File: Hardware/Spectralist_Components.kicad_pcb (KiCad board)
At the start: 4 copper layers, 70.8 x 100 mm, 98 parts, among them J1 Conn_01x12_Pin, J2 Conn_01x12_Pin, J3 Conn_01x10_Pin, J4 Conn_01x10_Pin, J5 Eurorack_10_pin_power, J6 SWD_Header, J7 Conn_01x02_Pin, U1 STM32H7B0VBTx, U2 PCM5100APW, U3 TPS561201, U4 LT1117-3.3, U5 MCP6002, U6 MX25LM51245G, U7 MCP6004, U8 TL072, Y1 8MHz 20pF

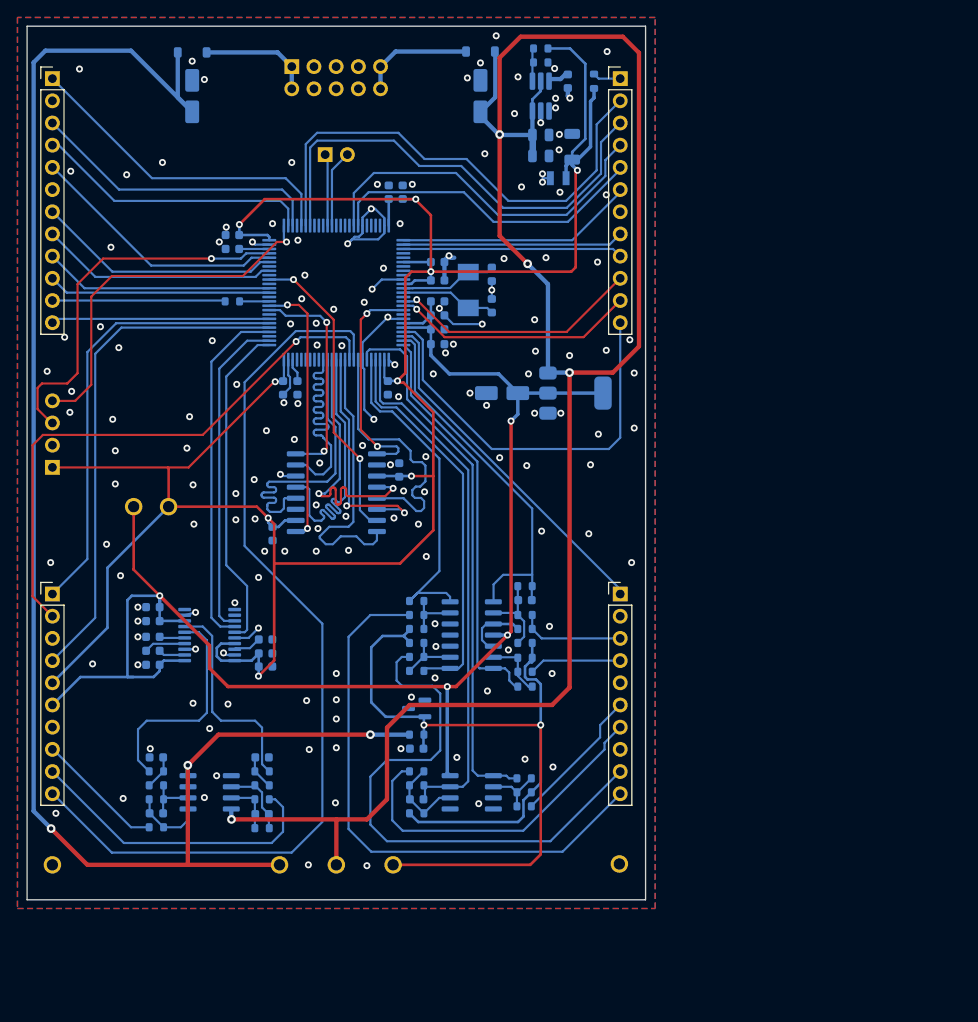
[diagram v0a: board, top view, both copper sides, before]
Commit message: Component PCB updates
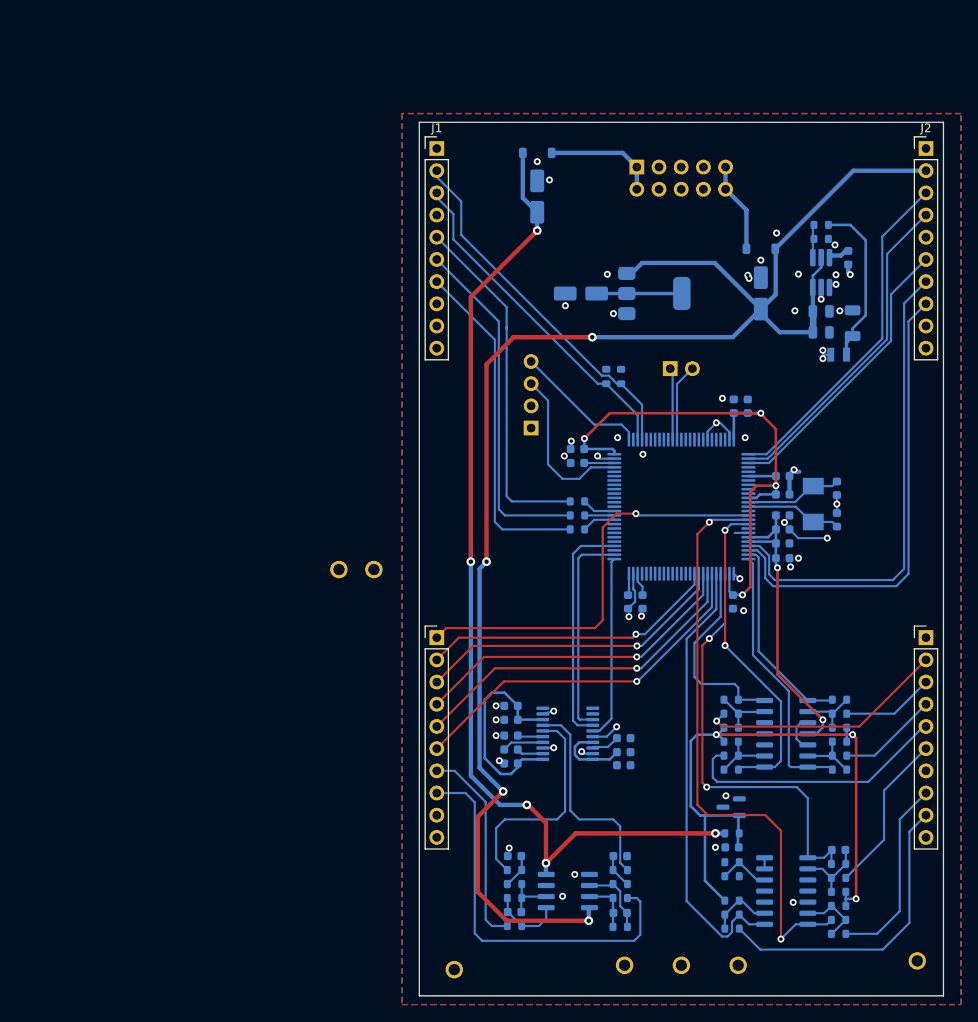
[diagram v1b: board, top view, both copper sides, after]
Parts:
- removed C33, C34: 100nF, Capacitor_SMD:C_0603_1608Metric
- removed C37: 2.2nF, Capacitor_SMD:C_0603_1608Metric
- removed U6: MX25LM51245G, Package_SO:SOIC-16W_7.5x10.3mm_P1.27mm
- added R28: 1k6, Resistor_SMD:R_0603_1608Metric, B.Cu at (123.1, 79.1)
- added R29: 75k, Resistor_SMD:R_0603_1608Metric, B.Cu at (148.1, 119.3)
- added R35: 82k, Resistor_SMD:R_0603_1608Metric, B.Cu at (148.1, 117.7)
- added R36: 47k, Resistor_SMD:R_0603_1608Metric, B.Cu at (148.1, 116.1)
- added R37: 10k, Resistor_SMD:R_0603_1608Metric, B.Cu at (135.8, 136.3)
- added R38: 1k, Resistor_SMD:R_0603_1608Metric, B.Cu at (118.1, 93.4)
- added R39: 1k, Resistor_SMD:R_0603_1608Metric, B.Cu at (118.1, 96.6)
- J1, J2: value Conn_01x12_Pin -> Conn_01x10_Pin; footprint Connector_PinHeader_2.54mm:PinHeader_1x12_P2.54mm_Vertical -> Connector_PinHeader_2.54mm:PinHeader_1x10_P2.54mm_Vertical
- R15: value 22 -> 1k6
- R31: value 100k -> 75k
- R32: value 20k -> 82k
- R33: value 33k -> 47k
- R34: value 6k8 -> 10k
- U1: value STM32H7B0VBTx -> STM32H723VGTx
- U5: value MCP6002 -> MCP6004; footprint Package_SO:SOIC-8_3.9x4.9mm_P1.27mm -> Package_SO:SO-14_3.9x8.65mm_P1.27mm
- moved J6 55.0 mm to (112.8, 85.0)
- moved R23 49.8 mm to (148.0, 136.5), turned to 0 degrees
- moved R22 49.1 mm to (148.0, 138.1), turned to 0 degrees
- moved R24 49.1 mm to (148.0, 134.9), turned to 0 degrees
- moved C35 48.6 mm to (148.0, 133.3), turned to 0 degrees
- moved TP4 47.5 mm to (104.0, 147.0)
- moved C14 46.5 mm to (147.8, 91.9)
- moved C15 46.5 mm to (147.8, 95.5)
- moved C21 46.5 mm to (118.1, 87.4)
- moved C16 46.5 mm to (137.6, 82.5)
- moved C17 46.5 mm to (141.6, 90.5)
- moved C18 46.5 mm to (141.6, 92.6)
- moved C19 46.5 mm to (135.9, 104.9)
- moved C20 46.5 mm to (123.9, 104.9)
- moved C22 46.5 mm to (136.0, 82.5)
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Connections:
- net /LED_Oct_B renamed /LED_Oct
- net /WarpCV renamed /Filter_B_CV
- net /Warp_CV_In renamed /Filter_B_CV_In
- net /Wavetable_Pos_A_Pot renamed /Harm_Stretch_Pot
- C35 pad 2: Net-(U5B--) -> Net-(U5A--)
- J1 pad 1: /LCD_SPI3_MOSI -> GND
- J1 pad 10: /Encoder_Up -> unconnected-(J1-Pin_10-Pad10)
- J1 pad 2: GND -> /I2C5_SCL
- J1 pad 3: /LCD_SPI3_SCK -> /I2C5_SDA
- J1 pad 4: /LCD_SPI3_SS -> GND
- J1 pad 5: /USB_DP -> /LED_Filter_A_Out
- J1 pad 6: GND -> /LED_Oct_Out
- J1 pad 7: /USB_DM -> /LED_Filter_B_Out
- J1 pad 8: /USB_VBUS -> unconnected-(J1-Pin_8-Pad8)
- J1 pad 9: /Encoder_Down -> unconnected-(J1-Pin_9-Pad9)
- J2 pad 1: /LCD_Backlight -> +3.3V
- J2 pad 10: /Warp_Amt_Trm -> unconnected-(J2-Pin_10-Pad10)
- J2 pad 2: /Octave_Up -> +12V
- J2 pad 3: /Octave_Down -> /Filter_Mode
- J2 pad 4: /LCD_DC -> /Warp_Mode
- J2 pad 5: /LCD_RESET -> GND
- J2 pad 6: /Mode -> /Octave_Btn
- J2 pad 7: GND -> /Filter_A_Trm
- J2 pad 8: /Warp_Polarity_Btn -> /Filter_A_Pot
- J2 pad 9: /Encoder_Btn -> unconnected-(J2-Pin_9-Pad9)
- J3 pad 1: /ChB_RM -> /Harm_Warp_Pot
- J3 pad 10: /Warp_Type_Pot -> unconnected-(J3-Pin_10-Pad10)
- J3 pad 3: GND -> /Harm_Stretch_Trm
- J3 pad 4: /ChB_Mix -> /Filter_Slope_Pot
- J3 pad 5: +3.3V -> /Filter_B_Trm
- J3 pad 6: +3.3VA -> /Filter_B_Pot
- J3 pad 7: GND -> /Audio_Out_L
- J3 pad 8: /Audio_Out_L -> /Audio_Out_R
- J3 pad 9: /Audio_Out_R -> unconnected-(J3-Pin_9-Pad9)
- J4 pad 1: /Wavetable_Pos_A_Trm -> unconnected-(J4-Pin_1-Pad1)
- J4 pad 10: /VCA_CV_In -> unconnected-(J4-Pin_10-Pad10)
- J4 pad 2: GND -> /Harm_Stretch_CV_In
- J4 pad 3: /Ext_Audio_In -> /Filter_A_CV_In
- J4 pad 5: GND -> /Filter_Slope_CV_In
- J4 pad 6: /Wavetable_Pos_A_CV_In -> /Pitch_CV_In
- J4 pad 7: /Pitch_CV_In -> unconnected-(J4-Pin_7-Pad7)
- J4 pad 8: GND -> /Harm_Warp_CV_In
- J4 pad 9: /Wavetable_Pos_B_CV_In -> /Pan_CV_In
- R12 pad 2: /Wavetable_Pos_B_CV_In -> /Filter_Slope_CV_In
- R15 pad 2: /LCD_Backlight -> /I2C5_SDA
- R16 pad 1: Net-(U5A--) -> Net-(U5B--)
- R17 pad 1: Net-(U5A--) -> Net-(U5B--)
- R17 pad 2: /Wavetable_Pos_A_CV_In -> /Harm_Warp_CV_In
- R19 pad 1: /WavetablePosA_CV -> /Harm_Warp_CV
- R19 pad 2: Net-(U5A--) -> Net-(U5B--)
- R21 pad 1: /WavetablePosB_CV -> /Filter_Slope_CV
- R22 pad 1: Net-(U5B--) -> Net-(U5A--)
- R23 pad 1: Net-(U5B--) -> Net-(U5A--)
- R24 pad 2: Net-(U5B--) -> Net-(U5A--)
- R26 pad 2: /VCA_CV_In -> /Harm_Stretch_CV_In
- R27 pad 1: /VcaCV -> /Harm_Stretch_CV
- R30 pad 2: /LED_Oct_B_Out -> /LED_Oct_Out
- R31 pad 1: /Ext_Audio_In -> Net-(U5C--)
- R31 pad 2: GND -> /-5V_REF
- R32 pad 1: Net-(U7A--) -> Net-(U5C--)
- R32 pad 2: /-5V_REF -> /Pan_CV_In
- R33 pad 1: Net-(U7A--) -> /Pan_CV
- R33 pad 2: /Ext_Audio_In -> Net-(U5C--)
- R34 pad 1: /AudioIn -> Net-(U5D-+)
- R34 pad 2: Net-(U7A--) -> +3.3V
- U1 pad 1: /Mode -> /Filter_Mode
- U1 pad 15: /Warp_Amt_Trm -> /Harm_Warp_Pot
- U1 pad 16: /Warp_Amt_Pot -> /Harm_Warp_CV
- U1 pad 17: /OCTOSPIM_P1_IO2 -> /Filter_Slope_CV
- U1 pad 2: /Warp_Polarity_Btn -> /Warp_Mode
- U1 pad 22: /Wavetable_Pos_B_Pot -> /Filter_A_Trm
- U1 pad 23: /Wavetable_Pos_A_Trm -> /Filter_A_Pot
- U1 pad 24: /AudioIn -> /Filter_A_CV
- U1 pad 29: /WavetablePosB_CV -> /Harm_Stretch_CV
- U1 pad 3: /Encoder_Btn -> /Octave_Btn
- U1 pad 30: /VcaCV -> /Pan_CV
- U1 pad 31: /WavetablePosA_CV -> /Filter_B_Pot
- U1 pad 32: GND -> /Filter_B_Trm
- U1 pad 33: /OCTOSPIM_P1_DQS -> /Filter_Slope_Pot
- U1 pad 34: /Warp_Type_Pot -> /Harm_Stretch_Trm
- U1 pad 36: /OCTOSPIM_P1_CLK -> unconnected-(U1-PB2-Pad36)
- U1 pad 37: /OCTOSPIM_P1_IO4 -> unconnected-(U1-PE7-Pad37)
- U1 pad 38: /OCTOSPIM_P1_IO5 -> unconnected-(U1-PE8-Pad38)
- U1 pad 39: /OCTOSPIM_P1_IO6 -> unconnected-(U1-PE9-Pad39)
- U1 pad 40: /OCTOSPIM_P1_IO7 -> unconnected-(U1-PE10-Pad40)
- U1 pad 41: /OCTOSPIM_P1_NCS -> unconnected-(U1-PE11-Pad41)
- U1 pad 55: /ChB_Mix -> unconnected-(U1-PD8-Pad55)
- U1 pad 56: /ChB_RM -> unconnected-(U1-PD9-Pad56)
- U1 pad 57: /B_Octave_Btn -> unconnected-(U1-PD10-Pad57)
- U1 pad 59: /OCTOSPIM_P1_IO1 -> unconnected-(U1-PD12-Pad59)
- U1 pad 60: /OCTOSPIM_P1_IO3 -> /LED_Filter_B
- U1 pad 62: unconnected-(U1-PD15-Pad62) -> /LED_Filter_A
- U1 pad 63: /Encoder_Up -> unconnected-(U1-PC6-Pad63)
- U1 pad 64: /Encoder_Down -> unconnected-(U1-PC7-Pad64)
- U1 pad 66: /OCTOSPIM_P1_IO0 -> unconnected-(U1-PC9-Pad66)
- U1 pad 77: /LCD_SPI3_SS -> unconnected-(U1-PA15(JTDI)-Pad77)
- U1 pad 78: /LCD_SPI3_SCK -> /I2C5_SDA
- U1 pad 79: unconnected-(U1-PC11-Pad79) -> /I2C5_SCL
- U1 pad 80: /LCD_SPI3_MOSI -> unconnected-(U1-PC12-Pad80)
- U1 pad 81: /Octave_Up -> unconnected-(U1-PD0-Pad81)
- U1 pad 82: /Octave_Down -> unconnected-(U1-PD1-Pad82)
- U1 pad 92: /LCD_DC -> unconnected-(U1-PB6-Pad92)
- U1 pad 93: /LCD_RESET -> unconnected-(U1-PB7-Pad93)
- U5 pad 1: /WavetablePosA_CV -> /Pitch_CV_Scaled
- U5 pad 4: GND -> +3.3VA
- U5 pad 7: /Pitch_CV_Scaled -> /Harm_Warp_CV
- U5 pad 8: +3.3VA -> /Pan_CV
- U7 pad 1: /AudioIn -> /Filter_A_CV
- U7 pad 14: /VcaCV -> /Harm_Stretch_CV
- U7 pad 8: /WavetablePosB_CV -> /Filter_Slope_CV
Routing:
- net +3.3V: track 282.4 -> 99.4 mm, vias 9 -> 4
- net /Warp_Type_Pot: track 107.1 -> 0.00 mm
- net +3.3VA: track 171.3 -> 69.6 mm, vias 4 -> 2
- net -12V: track 185.0 -> 113.8 mm, vias 3 -> 5
- net /Harm_Warp_CV: track 0.00 -> 67.4 mm, vias 0 -> 2
- net /VCA_CV_In: track 65.0 -> 0.00 mm
- net /Wavetable_Pos_B_CV_In: track 63.4 -> 0.00 mm
- net /WavetablePosA_CV: track 61.9 -> 0.00 mm
- net /ChB_Mix: track 58.3 -> 0.00 mm
- net /Octave_Up: track 56.9 -> 0.00 mm
- net /Filter_A_Trm: track 0.00 -> 55.1 mm
- net /Octave_Down: track 54.1 -> 0.00 mm
- net /Filter_A_Pot: track 0.00 -> 53.7 mm
- net /Pan_CV: track 0.00 -> 51.7 mm
- net /ChB_RM: track 51.5 -> 0.00 mm
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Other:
- board size 70.8 x 100 mm -> 60 x 100 mm
- board text added: "Spectralist v1.0 2025 Mountjoy Modular and Tal Shoshani"
- board text removed: "Kishoof v1.0 2024 Mountjoy Modular and Tal Shoshani"

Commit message: Started adding USB
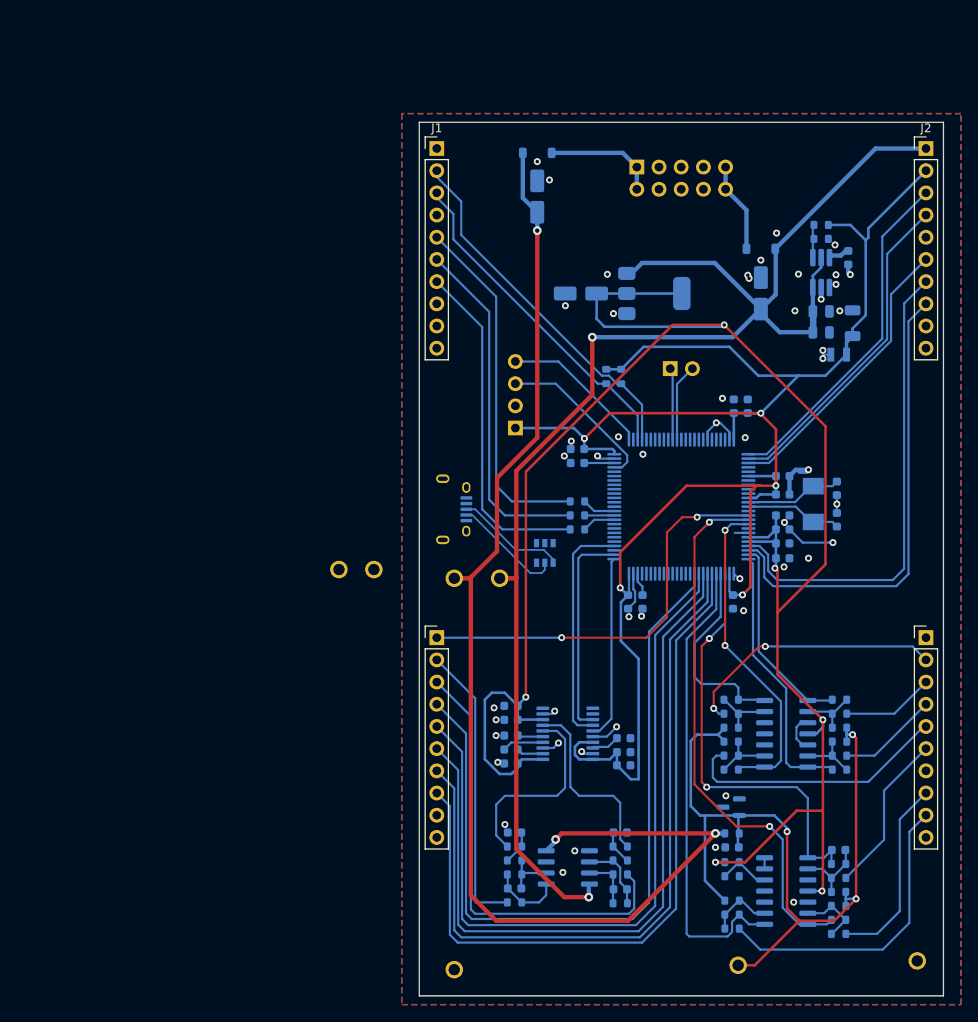
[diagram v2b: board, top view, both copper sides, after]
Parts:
- added J8: USB_B_Micro, Custom_Footprints:USB_Micro-B_Amphenol, B.Cu at (104.0, 94.3)
- added U6: STF202-22T1G, Custom_Footprints:STF202-22T1G, B.Cu at (114.4, 99.3)
- moved TP2 48.9 mm to (109.2, 102.2)
- moved TP3 48.4 mm to (104.0, 102.2)
- moved C31 2.70 mm to (110.9, 137.7)
- moved R10 2.70 mm to (123.0, 136.1)
- moved R7 2.70 mm to (110.9, 136.1)
- moved C29 2.70 mm to (110.9, 131.3)
- moved C30 2.70 mm to (123.0, 131.3)
- moved C32 2.70 mm to (123.0, 137.8)
- moved R3 2.70 mm to (110.9, 132.9)
- moved R4 2.70 mm to (123.0, 132.9)
- moved R5 2.70 mm to (110.9, 134.5)
- moved R6 2.70 mm to (123.0, 134.5)
- moved R8 2.70 mm to (123.0, 139.4)
- moved R9 2.70 mm to (110.9, 139.3)
- moved U8 2.70 mm to (117.0, 135.3)
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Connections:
- J2 pad 1: +3.3V -> +12V
- J2 pad 2: +12V -> +3.3V
- J3 pad 2: /Harm_Stretch_Pot -> /Audio_Out_L
- J3 pad 3: /Harm_Stretch_Trm -> /Audio_Out_R
- J3 pad 4: /Filter_Slope_Pot -> /Harm_Stretch_Pot
- J3 pad 5: /Filter_B_Trm -> /Harm_Stretch_Trm
- J3 pad 6: /Filter_B_Pot -> /Filter_Slope_Pot
- J3 pad 7: /Audio_Out_L -> /Filter_B_Trm
- J3 pad 8: /Audio_Out_R -> /Filter_B_Pot
- R34 pad 2: +3.3V -> +3.3VA
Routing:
- net +3.3VA: track 69.6 -> 221.6 mm, vias 2 -> 6
- net +3.3V: track 99.4 -> 207.1 mm, vias 4 -> 5
- net /Harm_Stretch_Pot: track 34.3 -> 87.1 mm, vias 1 -> 0
- net /Harm_Stretch_Trm: track 36.1 -> 86.6 mm, vias 1 -> 0
- net /Filter_Slope_Pot: track 38.1 -> 86.1 mm, vias 1 -> 0
- net /Filter_B_Trm: track 40.1 -> 85.5 mm, vias 1 -> 0
- net /Filter_B_Pot: track 42.0 -> 84.8 mm, vias 1 -> 0
- net -12V: track 113.8 -> 145.5 mm, vias 5 -> 3
- net /-5V_REF: track 73.1 -> 91.4 mm
- net +12V: track 174.7 -> 160.0 mm, vias 4 -> 2
- net /USB_D+: track 0.00 -> 12.7 mm
- net /USB_D-: track 0.00 -> 12.7 mm
- net /Audio_Out_L: track 23.3 -> 33.2 mm
- net /Audio_Out_R: track 44.8 -> 51.0 mm
- net /Harm_Warp_CV: track 67.4 -> 62.4 mm
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
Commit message: More layout on Component and Control boards
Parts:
- J1, J2: value Conn_01x10_Pin -> Conn_01x08_Pin; footprint Connector_PinHeader_2.54mm:PinHeader_1x10_P2.54mm_Vertical -> Connector_PinHeader_2.54mm:PinHeader_1x08_P2.54mm_Vertical
- moved TP5 73.1 mm to (153.0, 57.0)
- moved TP6 69.9 mm to (145.0, 57.0)
- moved TP2 60.2 mm to (149.0, 57.0)
- moved J8 57.6 mm to (130.0, 145.8), turned to 180 degrees
- moved TP3 56.9 mm to (139.0, 147.0)
- moved U6 11.9 mm to (107.9, 89.3)
- moved J3 10.0 mm to (102.0, 119.0)
- moved J4 10.0 mm to (158.0, 119.0)
- moved TP7 7.52 mm to (144.0, 147.0)
- moved J1 5.00 mm to (102.0, 58.0)
- moved J2 5.00 mm to (158.0, 58.0)
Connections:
- net /I2C5_SCL renamed /LED_SCL
- net /I2C5_SDA renamed /LED_SDA
- D3 pad 3: (no net) -> unconnected-(D3-NC-Pad3)
- J1 pad 7: /LED_Filter_B_Out -> GND
- J1 pad 8: unconnected-(J1-Pin_8-Pad8) -> /LED_Filter_B_Out
- J2 pad 1: +12V -> +3.3V
- J2 pad 2: +3.3V -> /Filter_Mode
- J2 pad 3: /Filter_Mode -> /Harmonic_Mode
- J2 pad 4: /Warp_Mode -> GND
- J2 pad 5: GND -> /Octave_Btn
- J2 pad 6: /Octave_Btn -> /Filter_A_Pot
- J2 pad 8: /Filter_A_Pot -> +12V
- J3 pad 1: /Harm_Warp_Pot -> /Filter_B_Trm
- J3 pad 10: unconnected-(J3-Pin_10-Pad10) -> /Harm_Warp_Pot
- J3 pad 3: /Audio_Out_R -> GND
- J3 pad 4: /Harm_Stretch_Pot -> /Audio_Out_R
- J3 pad 5: /Harm_Stretch_Trm -> /Filter_Slope_Pot
- J3 pad 6: /Filter_Slope_Pot -> /Filter_B_Pot
- J3 pad 7: /Filter_B_Trm -> GND
- J3 pad 8: /Filter_B_Pot -> /Harm_Stretch_Trm
- J3 pad 9: unconnected-(J3-Pin_9-Pad9) -> /Harm_Stretch_Pot
- J4 pad 1: unconnected-(J4-Pin_1-Pad1) -> GND
- J4 pad 10: unconnected-(J4-Pin_10-Pad10) -> /Filter_A_CV_In
- J4 pad 2: /Harm_Stretch_CV_In -> /Harm_Warp_CV_In
- J4 pad 3: /Filter_A_CV_In -> /Filter_B_CV_In
- J4 pad 4: /Filter_B_CV_In -> GND
- J4 pad 6: /Pitch_CV_In -> /Pan_CV_In
- J4 pad 7: unconnected-(J4-Pin_7-Pad7) -> GND
- J4 pad 8: /Harm_Warp_CV_In -> /Pitch_CV_In
- J4 pad 9: /Pan_CV_In -> /Harm_Stretch_CV_In
- J8 pad 1: unconnected-(J8-VBUS-Pad1) -> /USB_VBUS
- R12 pad 2: /Filter_Slope_CV_In -> /Pan_CV_In
- R13 pad 1: /Filter_B_CV -> /Filter_Slope_CV
- R17 pad 2: /Harm_Warp_CV_In -> /Harm_Stretch_CV_In
- R19 pad 1: /Harm_Warp_CV -> /Harm_Stretch_CV
- R20 pad 2: /Filter_B_CV_In -> /Filter_Slope_CV_In
- R21 pad 1: /Filter_Slope_CV -> /Pan_CV
- R26 pad 2: /Harm_Stretch_CV_In -> /Harm_Warp_CV_In
- R27 pad 1: /Harm_Stretch_CV -> /Harm_Warp_CV
- R32 pad 2: /Pan_CV_In -> /Filter_A_CV_In
- R33 pad 1: /Pan_CV -> /Filter_A_CV
- R35 pad 2: /Filter_A_CV_In -> /Filter_B_CV_In
- R36 pad 1: /Filter_A_CV -> /Filter_B_CV
- U1 pad 15: /Harm_Warp_Pot -> /Filter_B_Trm
- U1 pad 16: /Harm_Warp_CV -> /Harm_Stretch_CV
- U1 pad 17: /Filter_Slope_CV -> /Pan_CV
- U1 pad 2: /Warp_Mode -> /Harmonic_Mode
- U1 pad 22: /Filter_A_Trm -> /Filter_A_Pot
- U1 pad 23: /Filter_A_Pot -> /Filter_A_Trm
- U1 pad 24: /Filter_A_CV -> /Filter_B_CV
- U1 pad 25: /Filter_B_CV -> /Filter_Slope_CV
- U1 pad 29: /Harm_Stretch_CV -> /Harm_Warp_CV
- U1 pad 30: /Pan_CV -> /Filter_A_CV
- U1 pad 31: /Filter_B_Pot -> /Harm_Warp_Pot
- U1 pad 32: /Filter_B_Trm -> /Harm_Stretch_Pot
- U1 pad 33: /Filter_Slope_Pot -> /Harm_Stretch_Trm
- U1 pad 34: /Harm_Stretch_Trm -> /Filter_B_Pot
- U1 pad 35: /Harm_Stretch_Pot -> /Filter_Slope_Pot
- U5 pad 7: /Harm_Warp_CV -> /Harm_Stretch_CV
- U5 pad 8: /Pan_CV -> /Filter_A_CV
- U7 pad 1: /Filter_A_CV -> /Filter_B_CV
- U7 pad 14: /Harm_Stretch_CV -> /Harm_Warp_CV
- U7 pad 7: /Filter_B_CV -> /Filter_Slope_CV
- U7 pad 8: /Filter_Slope_CV -> /Pan_CV
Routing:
- net /USB_VBUS: track 0.00 -> 86.3 mm, vias 0 -> 2
- net /USB_D-: track 12.7 -> 85.3 mm, vias 0 -> 2
- net /USB_D+: track 12.7 -> 82.2 mm, vias 0 -> 2
- net /Harm_Warp_CV: track 62.4 -> 23.1 mm, vias 2 -> 0
- net /Harm_Stretch_CV: track 23.1 -> 62.4 mm, vias 0 -> 2
- net /Warp_Mode: track 37.6 -> 0.00 mm
- net /Harmonic_Mode: track 0.00 -> 35.8 mm
- net /Filter_A_CV: track 22.9 -> 53.9 mm
- net /Filter_B_Trm: track 85.5 -> 56.5 mm, vias 0 -> 2
- net +3.3VA: track 221.6 -> 246.4 mm
- net /Harm_Warp_Pot: track 47.2 -> 69.9 mm, vias 2 -> 0
- net /Harm_Stretch_CV_In: track 30.4 -> 10.7 mm, vias 2 -> 0
- net /Filter_Slope_CV_In: track 30.8 -> 11.8 mm
- net /Harm_Stretch_Pot: track 87.1 -> 70.4 mm
- net /Pan_CV: track 53.9 -> 37.3 mm, vias 0 -> 2
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
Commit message: More PCB Layout
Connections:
- J3 pad 1: /Filter_B_Trm -> /Filter_B_Pot
- J3 pad 6: /Filter_B_Pot -> /Filter_B_Trm
- U1 pad 15: /Filter_B_Trm -> /Filter_B_Pot
- U1 pad 34: /Filter_B_Pot -> /Filter_B_Trm
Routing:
- net /Filter_B_Pot: track 74.7 -> 55.2 mm, vias 0 -> 2
- net /Filter_B_Trm: track 56.5 -> 75.2 mm, vias 2 -> 0
- net /Filter_A_Trm: track 51.2 -> 48.8 mm
- net /Filter_A_Pot: track 52.5 -> 50.2 mm
- net /Audio_Out_L: track 23.2 -> 25.0 mm
- net /Audio_Out_R: track 38.5 -> 40.1 mm
- net /Filter_Slope_Pot: track 74.7 -> 75.9 mm
- net /Harm_Stretch_Trm: track 71.0 -> 71.8 mm
- net +3.3VA: track 246.4 -> 246.9 mm

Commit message: More PCB layout
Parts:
- moved J6 2.28 mm to (109.2, 83.6)
- moved C2 0.70 mm to (112.8, 58.5)
- moved D2 0.70 mm to (112.8, 53.5)
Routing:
- net GND: track 42.8 -> 38.1 mm
- net +3.3V: track 208.5 -> 210.9 mm
- net /SWIO: track 18.7 -> 21.1 mm
- net /SWCLK: track 17.0 -> 19.4 mm
- net /-12V_IN: track 13.0 -> 13.7 mm
